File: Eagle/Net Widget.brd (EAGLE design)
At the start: 66 x 45.7 mm, 17 parts, among them IC1 ATmega1284P

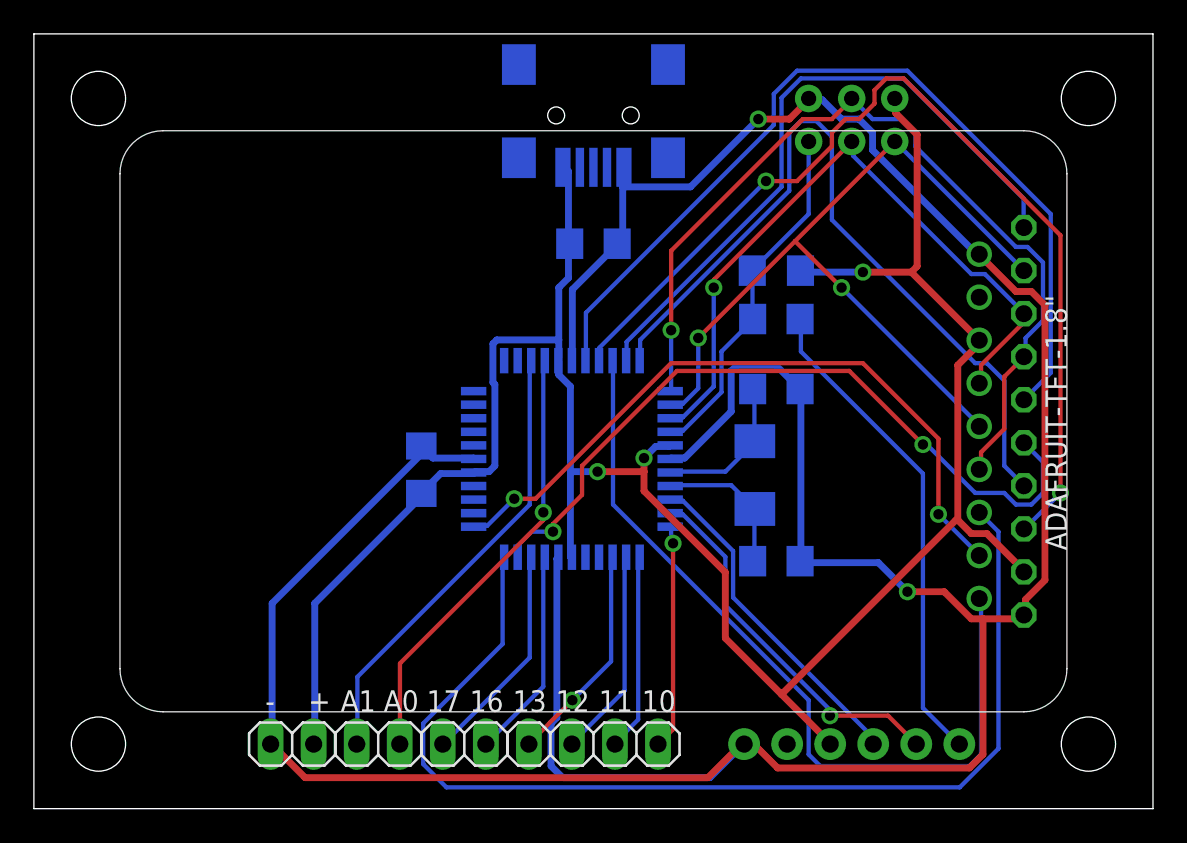
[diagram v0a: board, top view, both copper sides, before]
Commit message: SMD pads for breakout boards and layout.
Moved a bunch of things around after switching to right-angle
surface-mount headers for the CC3000 and TFT breakout boards.
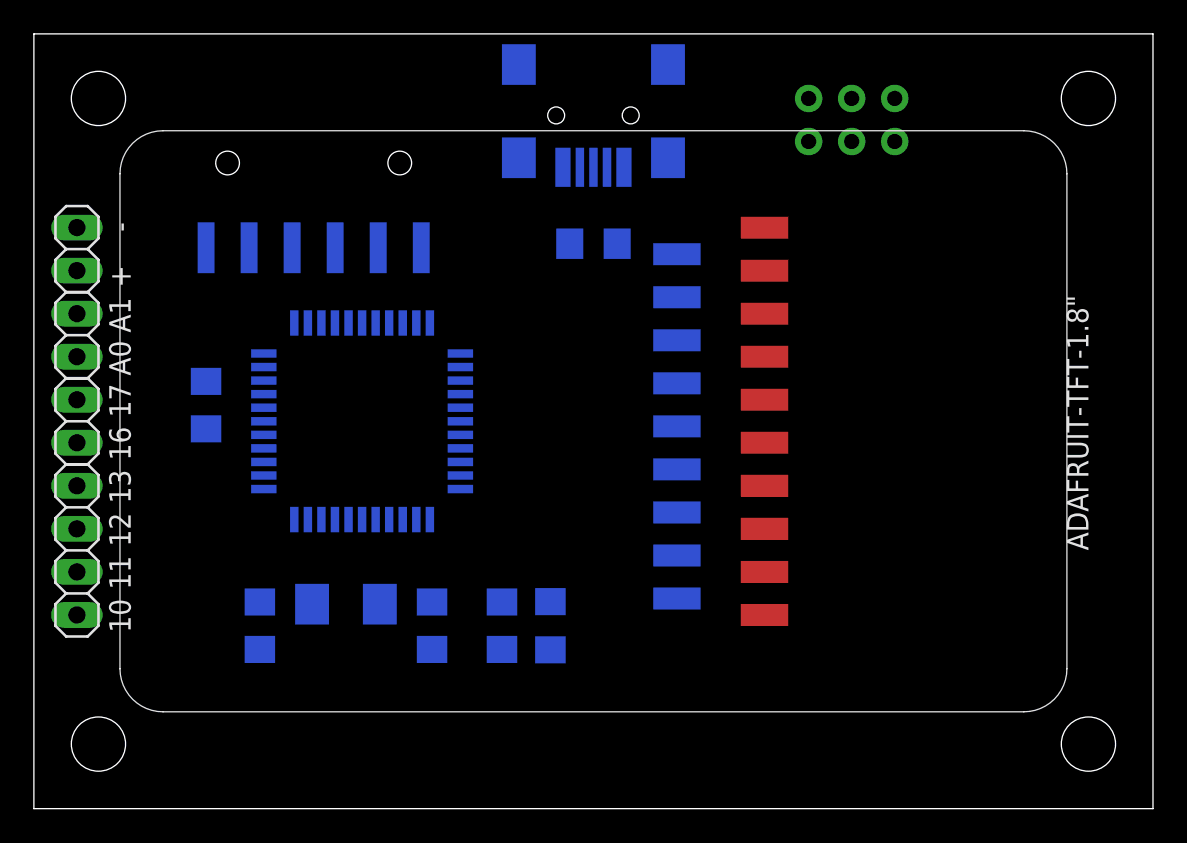
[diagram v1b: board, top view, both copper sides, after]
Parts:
- JP5: device Net Widget:1X06 -> SparkFun-Connectors:1X06-SMD
- U$2: value ADAFRUIT-CC3000-BREAKOUT -> ADAFRUIT-CC3000-BREAKOUTRA; device Net Widget:ADAFRUIT-CC3000-BREAKOUT -> Net Widget:ADAFRUIT-CC3000-BREAKOUT-RA
- U$3: value ADAFRUIT-TFT1.8-BREAKOUT -> ADAFRUIT-TFT1.8-BREAKOUT-RA; device Net Widget:ADAFRUIT-TFT1.8-BREAKOUT -> Net Widget:ADAFRUIT-TFT1.8-BREAKOUT-RA
- moved JP5 51.3 mm to (16.5, 38.1), turned to 180 degrees
- moved JP1 32.6 mm to (2.54, 15.2), turned to 90 degrees
- moved JP4 31.9 mm to (2.54, 33.0), turned to 90 degrees
- moved C2 30.7 mm to (13.3, 10.8), turned to 90 degrees
- moved JP2 30.0 mm to (2.54, 27.9), turned to 90 degrees
- moved JP3 29.8 mm to (2.54, 22.9), turned to 90 degrees
- moved 16MHZ 25.3 mm to (18.4, 12.1), turned to 180 degrees
- moved R4 24.8 mm to (30.5, 10.8), turned to 270 degrees
- moved C3 24.7 mm to (23.5, 10.8), turned to 90 degrees
- moved C1 24.3 mm to (27.6, 10.8), turned to 270 degrees
- moved C5 13.3 mm to (10.2, 23.8)
- moved IC1 12.6 mm to (19.4, 22.9), turned to 90 degrees
- moved U$2 2.54 mm to (55.2, 35.6)
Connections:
- net 3V3: now also U$2.P$2; no longer U$2.P2
- net CS: now also U$2.P$7; no longer U$2.P7
- net DTR: now also JP5.1; no longer JP5.DTR
- net GND: now also JP5.6, U$2.P$1; no longer JP5.GND, U$2.P1
- net IRQ: now also U$2.P$9; no longer U$2.P9
- net MISO: now also U$2.P$5; no longer U$2.P5
- net MOSI: now also U$2.P$6; no longer U$2.P6
- net RX: now also JP5.3; no longer JP5.TXO
- net SCK: now also U$2.P$4; no longer U$2.P4
- net TX: now also JP5.2; no longer JP5.RXI
- net VBEN: now also U$2.P$8; no longer U$2.P8
- net VCC: now also JP5.4, U$2.P$3; no longer JP5.VCC, U$2.P3
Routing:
- net GND: track 203.6 -> 0.00 mm, vias 2 -> 0
- net VCC: track 139.4 -> 0.00 mm, vias 3 -> 0
- net CS: track 64.1 -> 0.00 mm
- net TFT_RESET: track 57.6 -> 0.00 mm, vias 2 -> 0
- net TFT_CS: track 52.4 -> 0.00 mm
- net MOSI: track 52.3 -> 0.00 mm, vias 1 -> 0
- net IRQ: track 48.0 -> 0.00 mm
- net MISO: track 47.6 -> 0.00 mm, vias 2 -> 0
- net D/C: track 46.0 -> 0.00 mm
- net CARD_CS: track 44.2 -> 0.00 mm, vias 2 -> 0
- net SCK: track 41.2 -> 0.00 mm, vias 1 -> 0
- net VBEN: track 41.1 -> 0.00 mm, vias 2 -> 0
- net LITE: track 38.7 -> 0.00 mm
- net DTR: track 29.0 -> 0.00 mm
- net A1: track 26.9 -> 0.00 mm
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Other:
- board text added: "February 12, 2015"
- board text removed: "January 20, 2015"

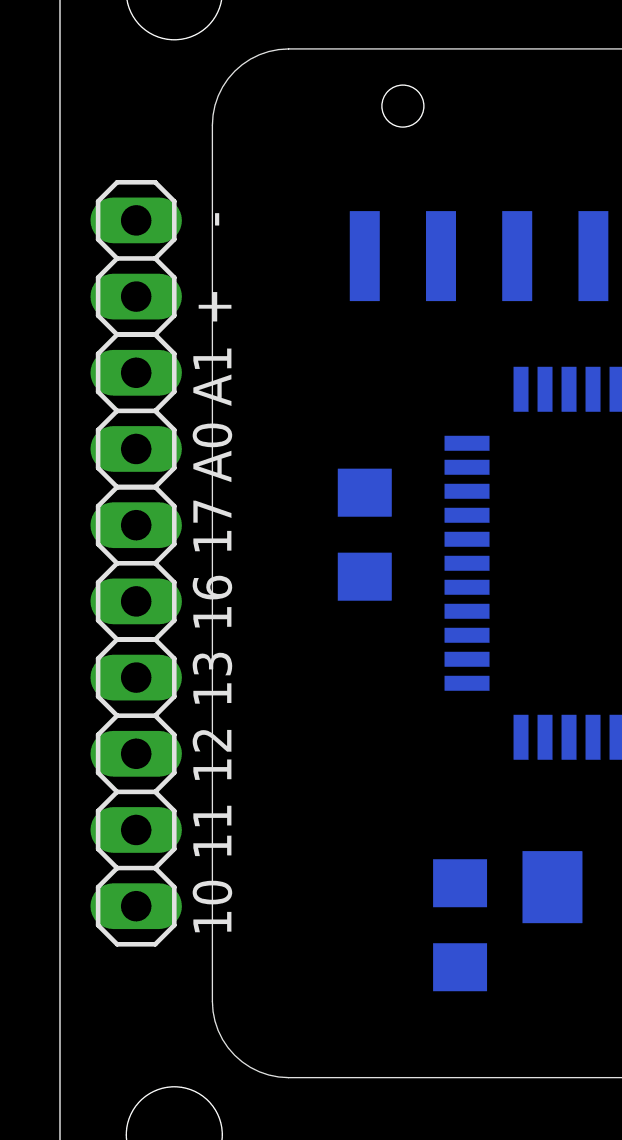
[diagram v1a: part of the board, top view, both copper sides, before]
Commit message: Remove broken-out pins.
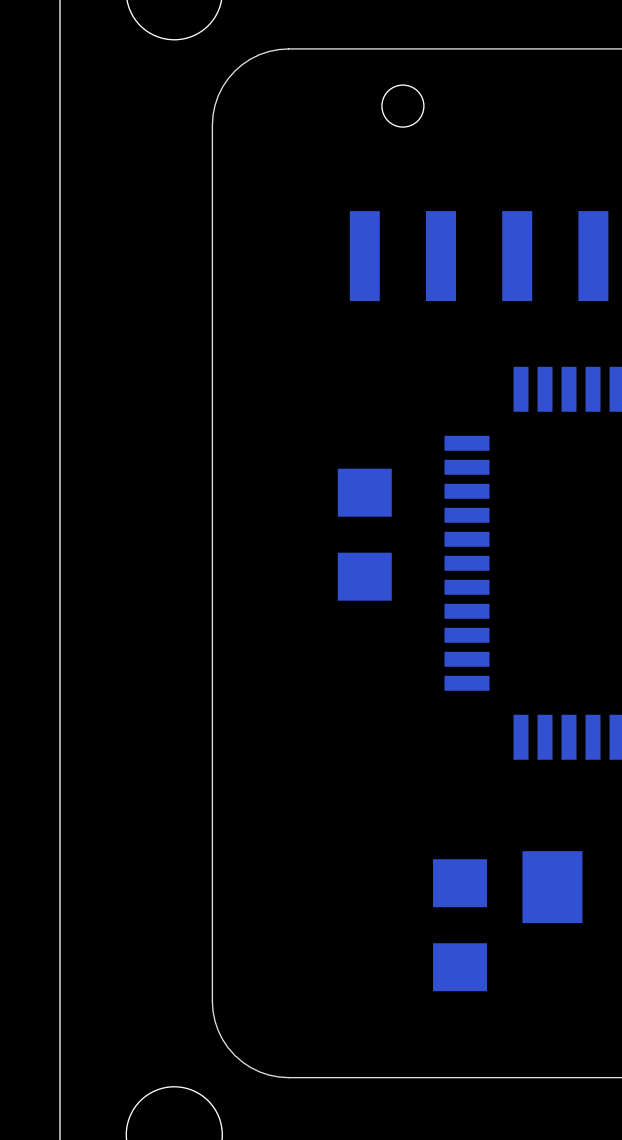
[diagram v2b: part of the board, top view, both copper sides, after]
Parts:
- removed JP1: (no value), pinhead:1X04
- removed JP2, JP3, JP4: (no value), pinhead:1X02
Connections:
- removed net 10: IC1.11, JP1.1
- removed net 11: IC1.12, JP1.2
- removed net 12: IC1.13, JP1.3
- removed net 13: IC1.14, JP1.4
- removed net 16: IC1.19, JP3.1
- removed net 17: IC1.20, JP3.2
- removed net A0: IC1.37, JP2.1
- removed net A1: IC1.36, JP2.2
- net GND: no longer JP4.2
- net VCC: no longer JP4.1
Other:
- board text removed: "+"
- board text removed: "-"
- board text removed: "10"
- board text removed: "11"
- board text removed: "12"
- board text removed: "13"
- board text removed: "16"
- board text removed: "17"
- board text removed: "A0"
- board text removed: "A1"
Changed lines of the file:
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@@
 <text x="59.69" y="1.27" size="1.778" layer="26" font="fixed" rot="MR0">DAVID A. MELLIS</text>
 <text x="33.02" y="1.27" size="1.778" layer="26" font="fixed" rot="MR0">February 12, 2015</text>
-<text x="4.445" y="12.3825" size="1.27" layer="25" font="fixed" rot="R270">10</text>
-<text x="4.445" y="10.4775" size="1.27" layer="26" font="fixed" rot="MR90">10</text>
-<text x="4.445" y="13.0175" size="1.27" layer="26" font="fixed" rot="MR90">11</text>
-<text x="4.445" y="14.9225" size="1.27" layer="25" font="fixed" rot="R270">11</text>
-<text x="4.445" y="17.4625" size="1.27" layer="25" font="fixed" rot="R270">12</text>
-<text x="4.445" y="15.5575" size="1.27" layer="26" font="fixed" rot="MR90">12</text>
-<text x="4.445" y="18.0975" size="1.27" layer="26" font="fixed" rot="MR90">13</text>
-<text x="4.445" y="20.0025" size="1.27" layer="25" font="fixed" rot="R270">13</text>
-<text x="4.445" y="22.5425" size="1.27" layer="25" font="fixed" rot="R270">16</text>
-<text x="4.445" y="20.6375" size="1.27" layer="26" font="fixed" rot="MR90">16</text>
-<text x="4.445" y="23.1775" size="1.27" layer="26" font="fixed" rot="MR90">17</text>
-<text x="4.445" y="25.0825" size="1.27" layer="25" font="fixed" rot="R270">17</text>
-<text x="4.445" y="27.6225" size="1.27" layer="25" font="fixed" rot="R270">A0</text>
-<text x="4.445" y="25.7175" size="1.27" layer="26" font="fixed" rot="MR90">A0</text>
-<text x="4.445" y="28.2575" size="1.27" layer="26" font="fixed" rot="MR90">A1</text>
-<text x="4.445" y="30.1625" size="1.27" layer="25" font="fixed" rot="R270">A1</text>
-<text x="4.445" y="34.6075" size="1.27" layer="25" font="fixed" rot="R270">-</text>
-<text x="4.445" y="33.9725" size="1.27" layer="26" font="fixed" rot="MR90">-</text>
-<text x="4.445" y="31.4325" size="1.27" layer="26" font="fixed" rot="MR90">+</text>
-<text x="4.445" y="32.0675" size="1.27" layer="25" font="fixed" rot="R270">+</text>
 <text x="25.0825" y="38.4175" size="1.27" layer="26" font="fixed" rot="MR180">B</text>
 <text x="7.3025" y="38.735" size="1.27" layer="26" font="fixed" rot="MR180">G</text>
@@
 <attribute name="NAME" x="15.875" y="15.24" size="1.27" layer="26" font="fixed" rot="MR180"/>
 </element>
-<element name="JP4" library="pinhead" package="1X02" value="" x="2.54" y="33.02" smashed="yes" rot="R90">
-<attribute name="VALUE" x="5.715" y="30.48" size="1.27" layer="27" rot="R90"/>
-</element>
 <element name="R4" library="rcl" package="R1206" value="10K" x="30.48" y="10.795" smashed="yes" rot="MR270">
 <attribute name="NAME" x="31.75" y="8.255" size="0.8128" layer="26" rot="MR270"/>
@@
 <attribute name="NAME" x="27.6225" y="8.255" size="0.8128" layer="26" rot="MR270"/>
 <attribute name="VALUE" x="29.5275" y="12.3825" size="1.016" layer="28" rot="MR270"/>
-</element>
-<element name="JP1" library="pinhead" package="1X04" value="" x="2.54" y="15.24" smashed="yes" rot="R90">
-<attribute name="VALUE" x="5.715" y="10.16" size="1.27" layer="27" rot="R90"/>
-</element>
-<element name="JP2" library="pinhead" package="1X02" value="" x="2.54" y="27.94" smashed="yes" rot="R90">
-<attribute name="VALUE" x="5.715" y="25.4" size="1.27" layer="27" rot="R90"/>
-</element>
-<element name="JP3" library="pinhead" package="1X02" value="" x="2.54" y="22.86" smashed="yes" rot="R90">
-<attribute name="VALUE" x="5.715" y="20.32" size="1.27" layer="27" rot="R90"/>
 </element>
 <element name="CN1" library="Net Widget" package="USB-MINIB-POWER" value="" x="33.02" y="43.18" rot="MR180"/>
@@
 <contactref element="C4" pad="2"/>
 <contactref element="C5" pad="2"/>
-<contactref element="JP4" pad="2"/>
 <contactref element="C3" pad="1"/>
 <contactref element="C2" pad="1"/>
@@
 <wire x1="23.495" y1="9.395" x2="19.3675" y2="17.06" width="0" layer="19" extent="16-16"/>
 <wire x1="13.335" y1="9.395" x2="19.3675" y2="17.06" width="0" layer="19" extent="16-16"/>
-<wire x1="2.54" y1="34.29" x2="13.335" y2="9.395" width="0" layer="19" extent="16-16"/>
 <wire x1="43.12" y1="11.43" x2="23.495" y2="9.395" width="0" layer="19" extent="1-16"/>
 </signal>
@@
 <contactref element="C4" pad="1"/>
 <contactref element="C5" pad="1"/>
-<contactref element="JP4" pad="1"/>
 <contactref element="IC1" pad="27"/>
 <contactref element="IC1" pad="5"/>
@@
 <wire x1="30.48" y1="9.373" x2="20.1675" y2="17.06" width="0" layer="19" extent="16-16"/>
 <wire x1="43.12" y1="13.97" x2="30.48" y2="9.373" width="0" layer="19" extent="1-16"/>
-<wire x1="2.54" y1="31.75" x2="20.1675" y2="17.06" width="0" layer="19" extent="16-16"/>
 </signal>
 <signal name="RESET">
@@
 <wire x1="13.335" y1="12.195" x2="16.415" y2="12.065" width="0" layer="19" extent="16-16"/>
 </signal>
-<signal name="A1">
-<contactref element="IC1" pad="36"/>
-<contactref element="JP2" pad="2"/>
-<wire x1="2.54" y1="29.21" x2="25.1675" y2="25.26" width="0" layer="19" extent="16-16"/>
-</signal>
-<signal name="A0">
-<contactref element="IC1" pad="37"/>
-<contactref element="JP2" pad="1"/>
-<wire x1="2.54" y1="26.67" x2="25.1675" y2="24.46" width="0" layer="19" extent="16-16"/>
-</signal>
 <signal name="AREF">
 <contactref element="IC1" pad="29"/>
@@
 <wire x1="16.1675" y1="17.06" x2="12.7" y2="33.1" width="0" layer="19" extent="16-16"/>
 </signal>
-<signal name="10">
-<contactref element="IC1" pad="11"/>
-<contactref element="JP1" pad="1"/>
-<wire x1="15.3675" y1="17.06" x2="2.54" y2="11.43" width="0" layer="19" extent="16-16"/>
-</signal>
-<signal name="11">
-<contactref element="IC1" pad="12"/>
-<contactref element="JP1" pad="2"/>
-<wire x1="13.5675" y1="18.86" x2="2.54" y2="13.97" width="0" layer="19" extent="16-16"/>
-</signal>
-<signal name="12">
-<contactref element="IC1" pad="13"/>
-<contactref element="JP1" pad="3"/>
-<wire x1="2.54" y1="16.51" x2="13.5675" y2="19.66" width="0" layer="19" extent="16-16"/>
-</signal>
-<signal name="13">
-<contactref element="IC1" pad="14"/>
-<contactref element="JP1" pad="4"/>
-<wire x1="2.54" y1="19.05" x2="13.5675" y2="20.46" width="0" layer="19" extent="16-16"/>
-</signal>
-<signal name="16">
-<contactref element="IC1" pad="19"/>
-<contactref element="JP3" pad="1"/>
-<wire x1="2.54" y1="21.59" x2="13.5675" y2="24.46" width="0" layer="19" extent="16-16"/>
-</signal>
-<signal name="17">
-<contactref element="IC1" pad="20"/>
-<contactref element="JP3" pad="2"/>
-<wire x1="2.54" y1="24.13" x2="13.5675" y2="25.26" width="0" layer="19" extent="16-16"/>
-</signal>
 </signals>

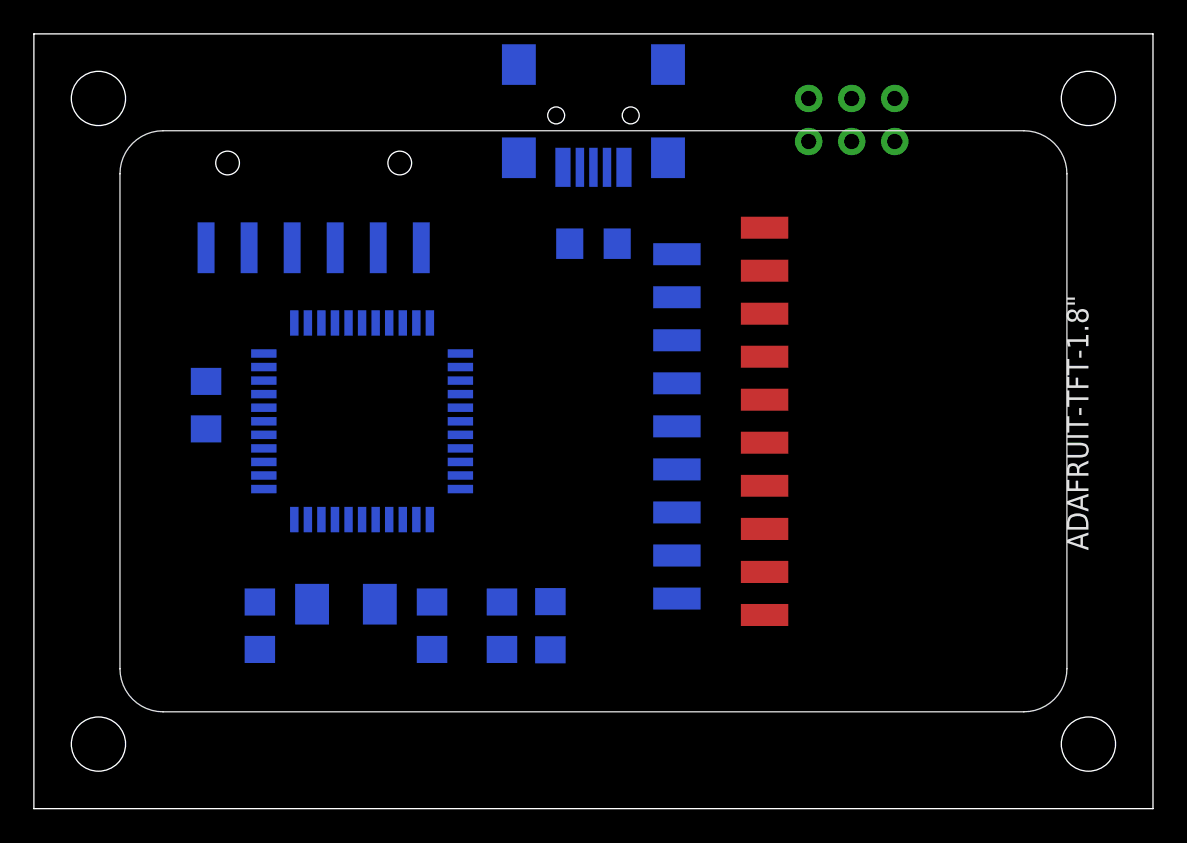
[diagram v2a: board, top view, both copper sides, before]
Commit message: Move CC3000, re-route, silk screen cleanup.
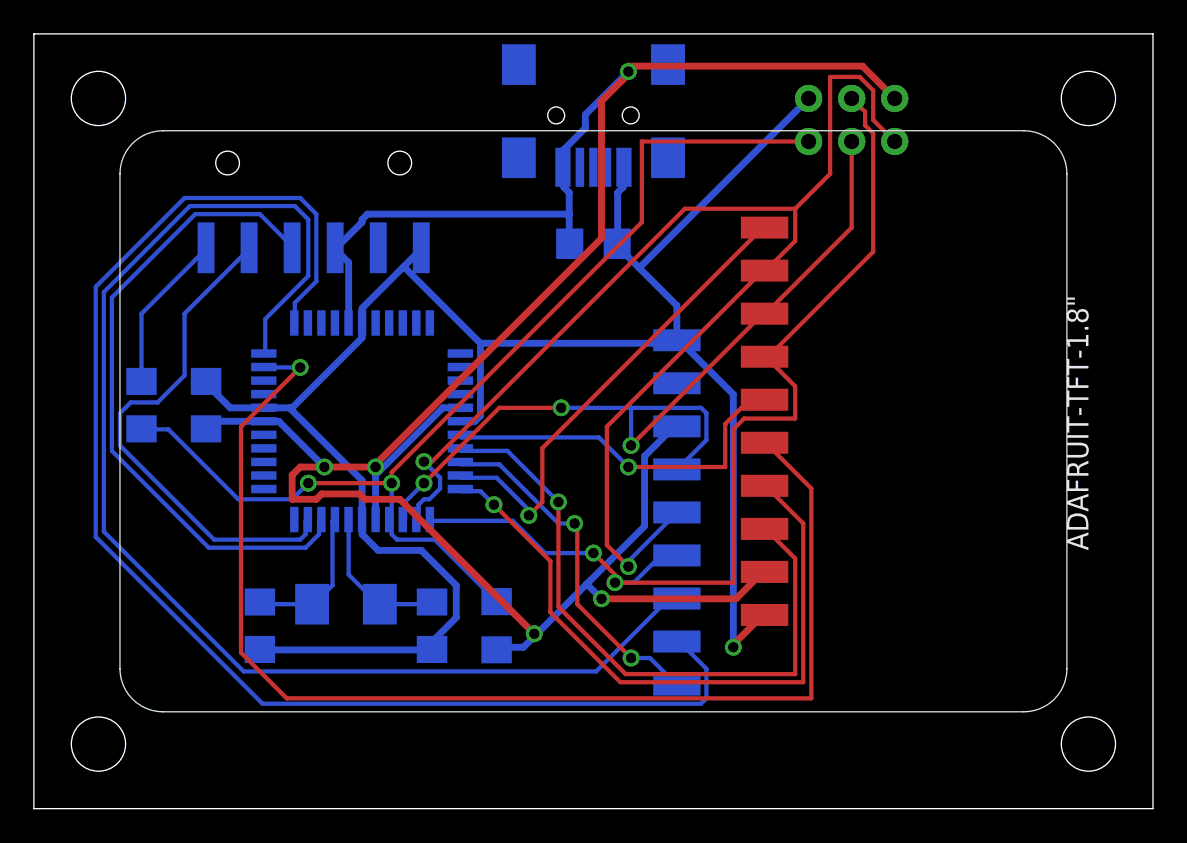
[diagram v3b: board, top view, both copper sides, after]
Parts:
- C2, C3: value 18pF -> 8pF
- moved C1 24.9 mm to (6.35, 23.8), turned to 90 degrees
- moved U$2 5.08 mm to (55.2, 30.5)
- moved R4 3.18 mm to (27.3, 10.8)
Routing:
- net VCC: track 0.00 -> 150.5 mm, vias 0 -> 5
- net GND: track 0.00 -> 121.0 mm, vias 0 -> 1
- net VBEN: track 0.00 -> 81.7 mm
- net MISO: track 0.00 -> 78.4 mm, vias 0 -> 2
- net CS: track 0.00 -> 76.6 mm
- net CARD_CS: track 0.00 -> 71.5 mm, vias 0 -> 1
- net RESET: track 0.00 -> 64.0 mm, vias 0 -> 2
- net MOSI: track 0.00 -> 60.1 mm, vias 0 -> 2
- net SCK: track 0.00 -> 51.0 mm, vias 0 -> 3
- net D/C: track 0.00 -> 39.3 mm, vias 0 -> 1
- net RX: track 0.00 -> 38.5 mm
- net TFT_RESET: track 0.00 -> 38.3 mm, vias 0 -> 1
- net TX: track 0.00 -> 30.1 mm
- net LITE: track 0.00 -> 28.0 mm, vias 0 -> 1
- net TFT_CS: track 0.00 -> 21.9 mm, vias 0 -> 1
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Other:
- board text added: "February 20, 2015"
- board text removed: "February 12, 2015"
